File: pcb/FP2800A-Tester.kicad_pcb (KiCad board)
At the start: 2 copper layers, 66 x 53.3 mm, 90 parts, among them SW1 Reset, U1 FP2800A

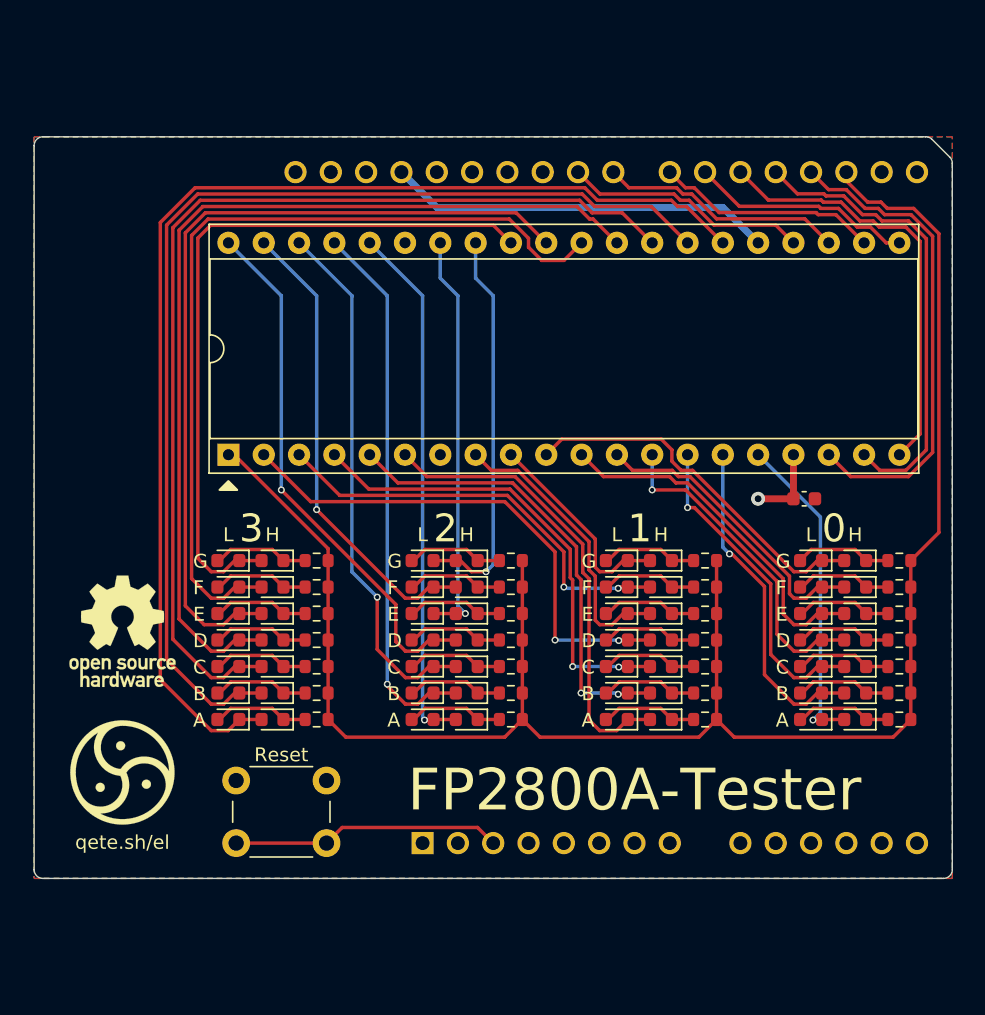
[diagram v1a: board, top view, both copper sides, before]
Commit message: feat: add rails
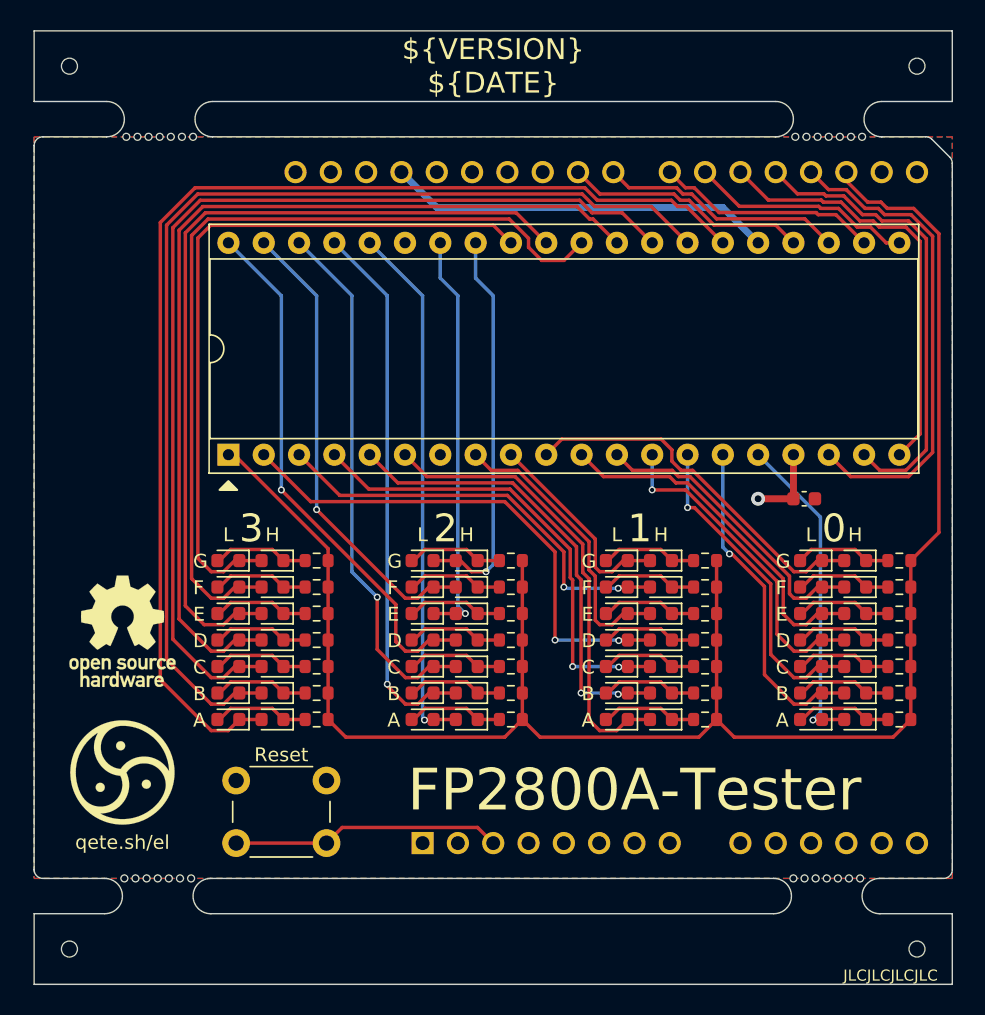
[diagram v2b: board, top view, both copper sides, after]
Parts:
- added REF**: mouse-bite-2.54mm-onesided, Panelization:mouse-bite-2.54mm-onesided, F.Cu at (151.1, 48.3)
- added REF**: JLCPCB_Tooling_Hole, My_Footprints:JLCPCB_Tooling_Hole, F.Cu at (96.5, 43.2)
- added REF**: mouse-bite-2.54mm-onesided, Panelization:mouse-bite-2.54mm-onesided, F.Cu at (103.0, 48.3)
- added REF**: mouse-bite-2.54mm-onesided, Panelization:mouse-bite-2.54mm-onesided, F.Cu at (151.0, 101.6)
- added REF**: JLCPCB_Tooling_Hole, My_Footprints:JLCPCB_Tooling_Hole, F.Cu at (157.5, 106.7)
- added REF**: JLCPCB_Tooling_Hole, My_Footprints:JLCPCB_Tooling_Hole, F.Cu at (96.5, 106.7)
- added REF**: JLCPCB_Tooling_Hole, My_Footprints:JLCPCB_Tooling_Hole, F.Cu at (157.5, 43.2)
- added REF**: mouse-bite-2.54mm-onesided, Panelization:mouse-bite-2.54mm-onesided, F.Cu at (102.9, 101.6)
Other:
- board size 66 x 53.3 mm -> 66 x 68.6 mm
- board text added: "${VERSION} ${DATE}"

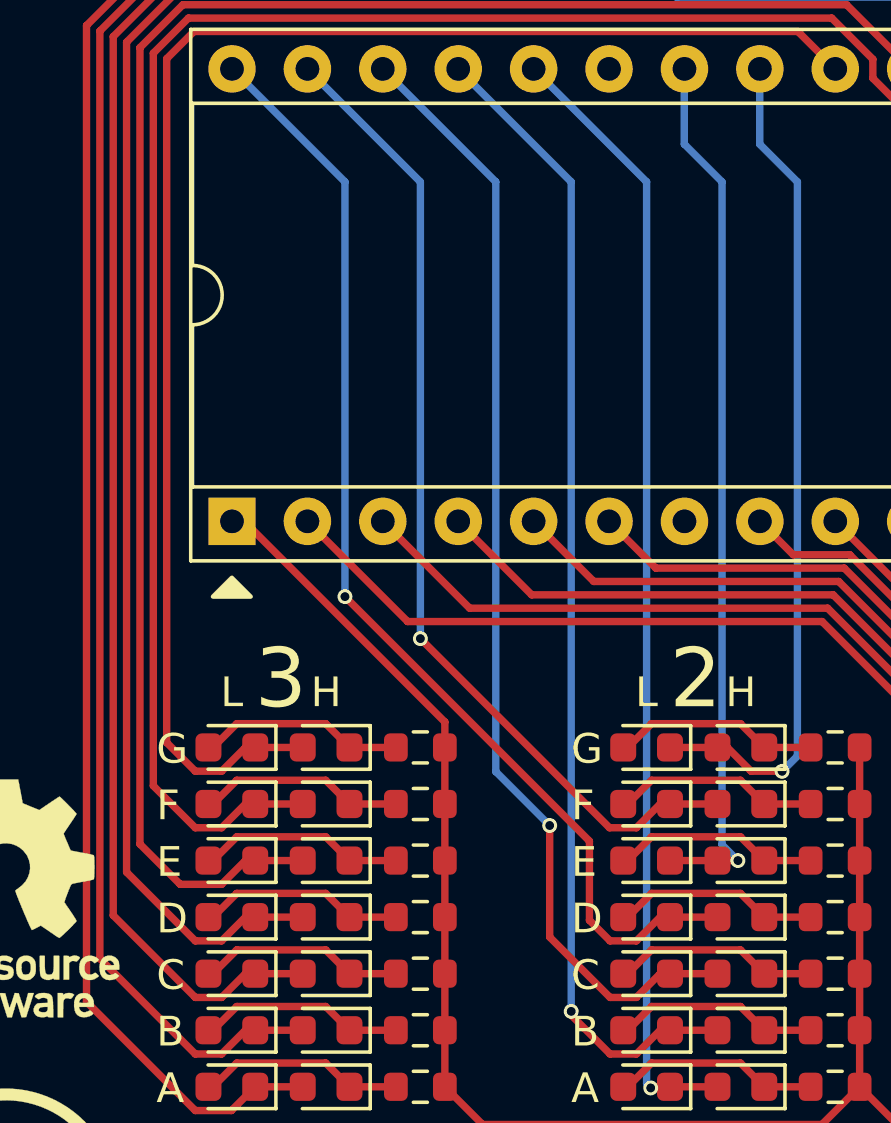
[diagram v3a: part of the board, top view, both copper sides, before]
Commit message: feat: add COM Jumper
Add a jumper that allows to disconnect the FP2800A COM pin from the LEDs
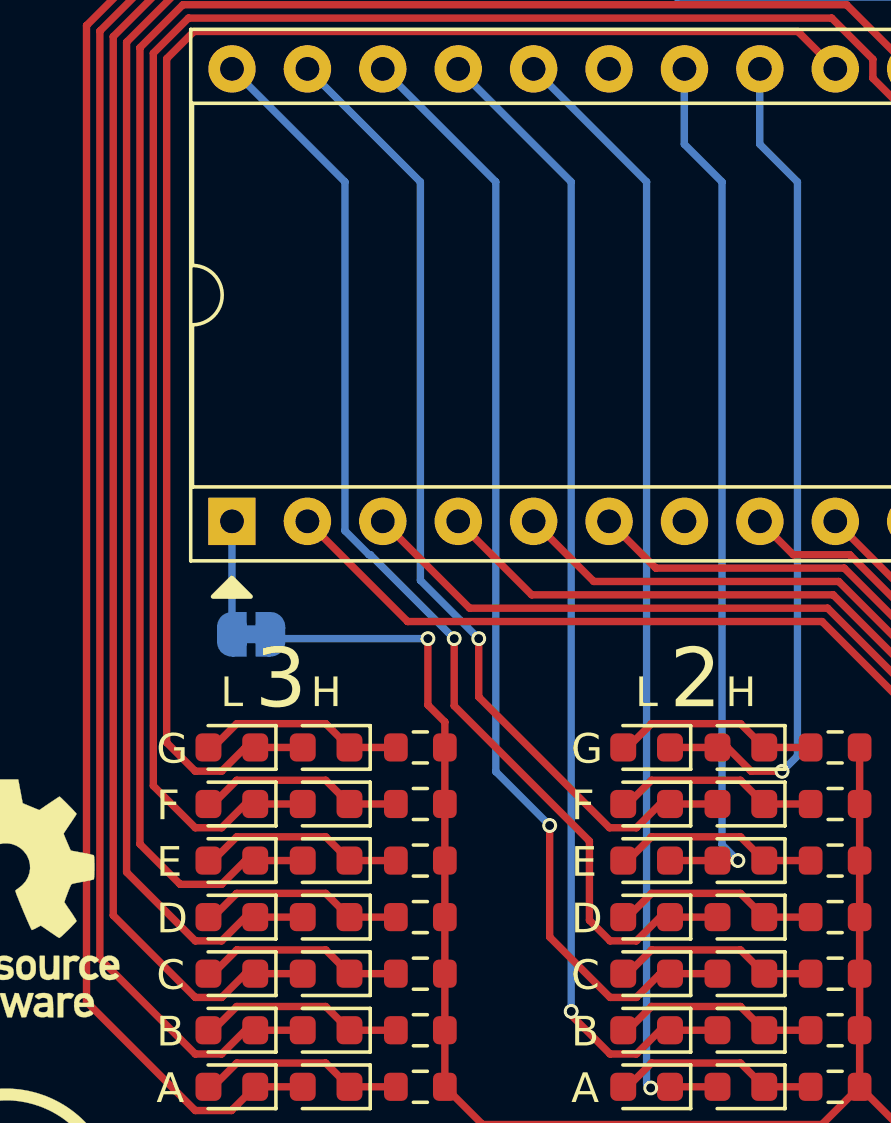
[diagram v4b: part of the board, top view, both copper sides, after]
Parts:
- added JP1: COM, Jumper:SolderJumper-2_P1.3mm_Bridged_RoundedPad1.0x1.5mm, B.Cu at (108.6, 74.9)
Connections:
- U1 pad 1: /COM -> Net-(JP1-B)
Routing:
- net Net-(JP1-B): track 0.00 -> 3.81 mm
- net /COM: track 134.8 -> 133.3 mm, vias 0 -> 1
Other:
- board text added: "COM"

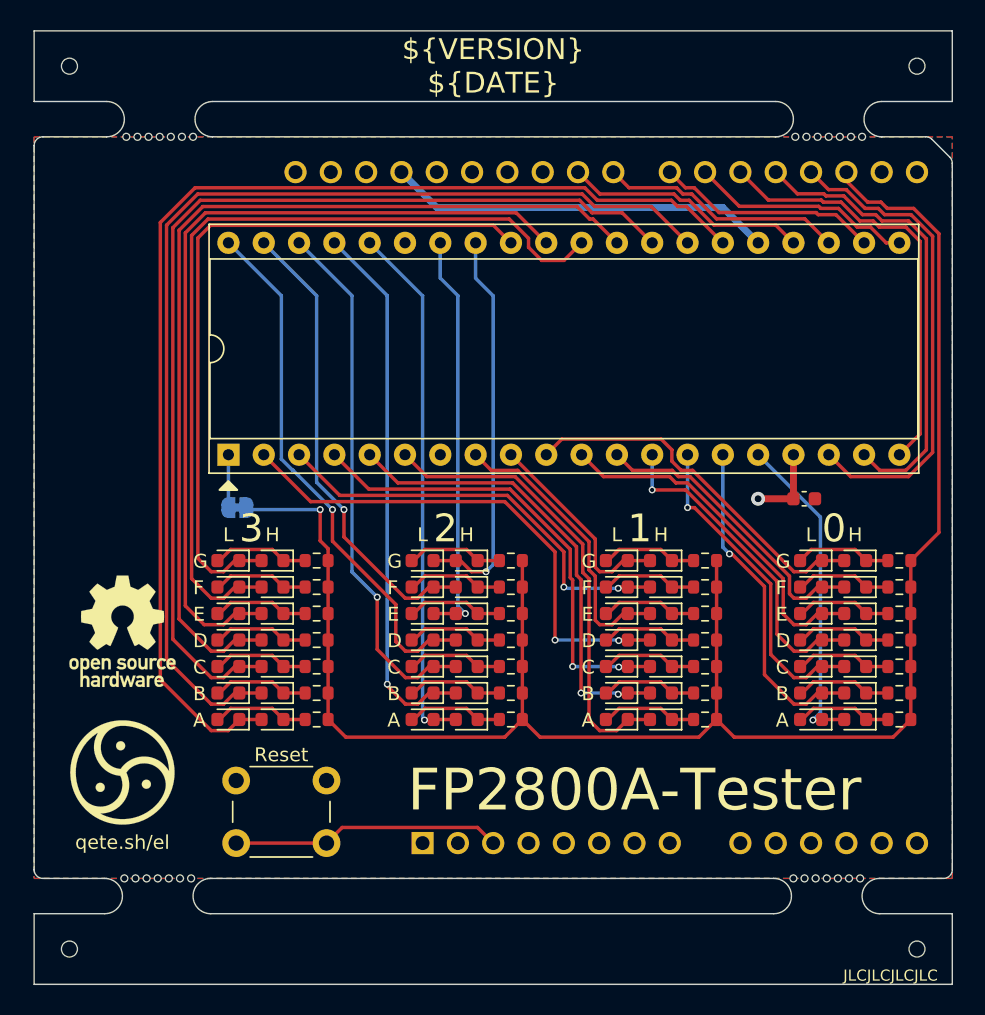
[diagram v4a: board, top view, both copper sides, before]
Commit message: feat: replace IC socket with ZIF socket
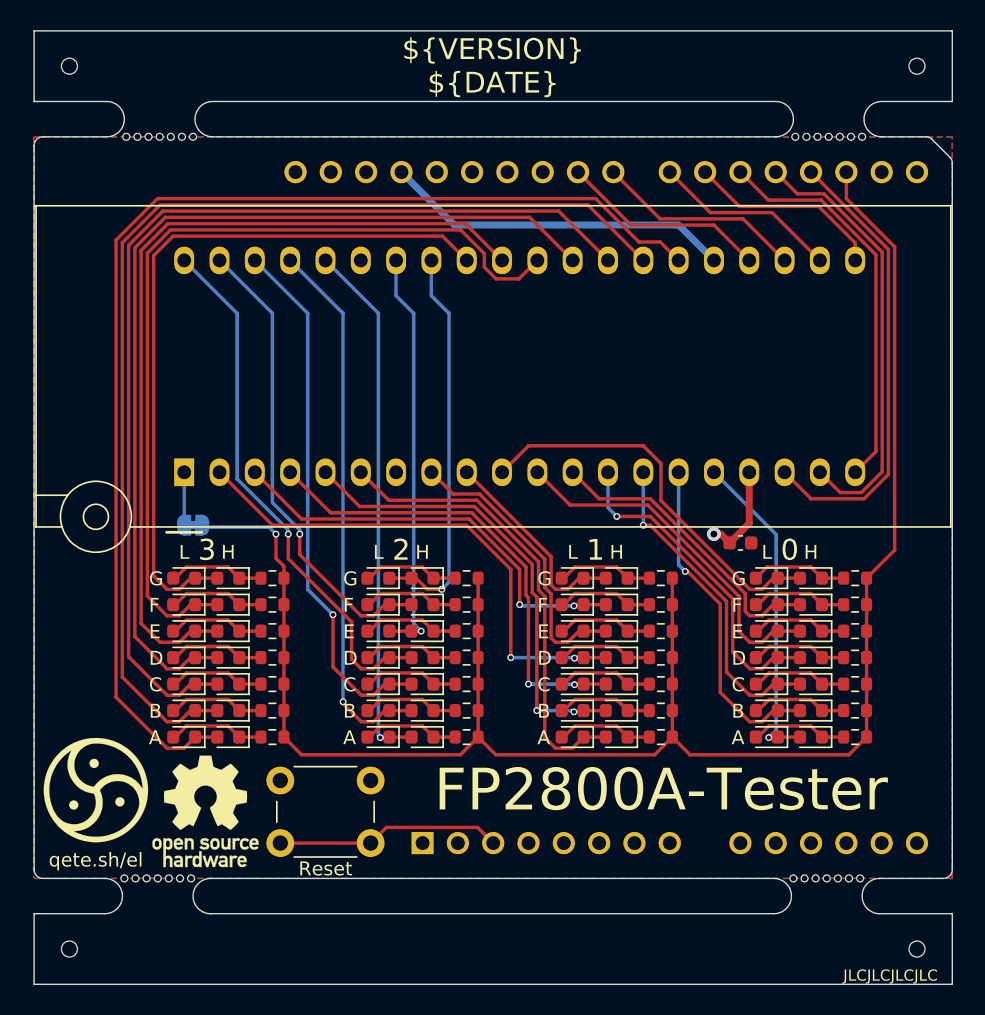
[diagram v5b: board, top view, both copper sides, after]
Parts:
- U1: footprint Package_DIP:DIP-40_W15.24mm_Socket -> Socket:DIP_Socket-40_W11.9_W12.7_W15.24_W17.78_W18.5_3M_240-1280-00-0602J
- moved REF** 14.3 mm to (106.3, 96.8)
- moved C1 5.58 mm to (144.8, 77.5)
- moved D1 3.42 mm to (149.9, 91.4)
- moved D10 3.42 mm to (146.7, 83.8)
- moved D11 3.42 mm to (149.9, 81.9)
- moved D12 3.42 mm to (146.7, 81.9)
- moved D13 3.42 mm to (149.9, 80.0)
- moved D14 3.42 mm to (146.7, 80.0)
- moved D15 3.42 mm to (135.9, 91.4)
- moved D17 3.42 mm to (135.9, 89.5)
- moved D19 3.42 mm to (135.9, 87.6)
- moved D2 3.42 mm to (146.7, 91.4)
- moved D21 3.42 mm to (135.9, 85.7)
- moved D23 3.42 mm to (135.9, 83.8)
- moved D25 3.42 mm to (135.9, 81.9)
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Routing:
- net /Reset: track 19.4 -> 16.2 mm
- net /B1: track 16.1 -> 13.4 mm
- net GND: track 27.8 -> 25.1 mm
- net /ENABLE: track 17.6 -> 14.9 mm
- net /DATA: track 17.6 -> 14.9 mm
- net /A2: track 30.9 -> 28.5 mm
- net /A0: track 33.6 -> 31.5 mm
- net /A1: track 35.0 -> 33.0 mm
- net /COM: track 133.3 -> 131.2 mm
- net /B0: track 16.1 -> 14.2 mm
- net /0G: track 26.7 -> 28.4 mm
- net +5V: track 5.71 -> 7.06 mm
- net /3F: track 61.3 -> 61.9 mm
